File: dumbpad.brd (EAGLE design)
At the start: 98 x 80 mm, 38 parts

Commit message: shrinking, aligning
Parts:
- moved D4 0.52 mm to (89.2, 77.0)
- moved D3 0.51 mm to (70.1, 77.0)
- moved D2 0.50 mm to (51.0, 77.0)
- moved D1 0.50 mm to (32.0, 77.0)
- moved D8 0.18 mm to (89.2, 58.6)
- moved D12 0.16 mm to (89.2, 39.5)
- moved D16 0.15 mm to (89.2, 20.5)
- moved D7 0.14 mm to (70.1, 58.6)
- moved D6 0.11 mm to (51.0, 58.6)
- moved D11 0.11 mm to (70.1, 39.5)
- moved D5 0.10 mm to (32.0, 58.6)
- moved D15 0.10 mm to (70.1, 20.5)
- moved D10 0.07 mm to (51.0, 39.5)
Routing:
- net N$1: track 12.9 -> 12.4 mm
- net N$2: track 12.9 -> 12.4 mm
- net N$3: track 12.9 -> 12.4 mm
- net N$4: track 12.9 -> 12.4 mm
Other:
- board size 98 x 80 mm -> 98 x 79.5 mm

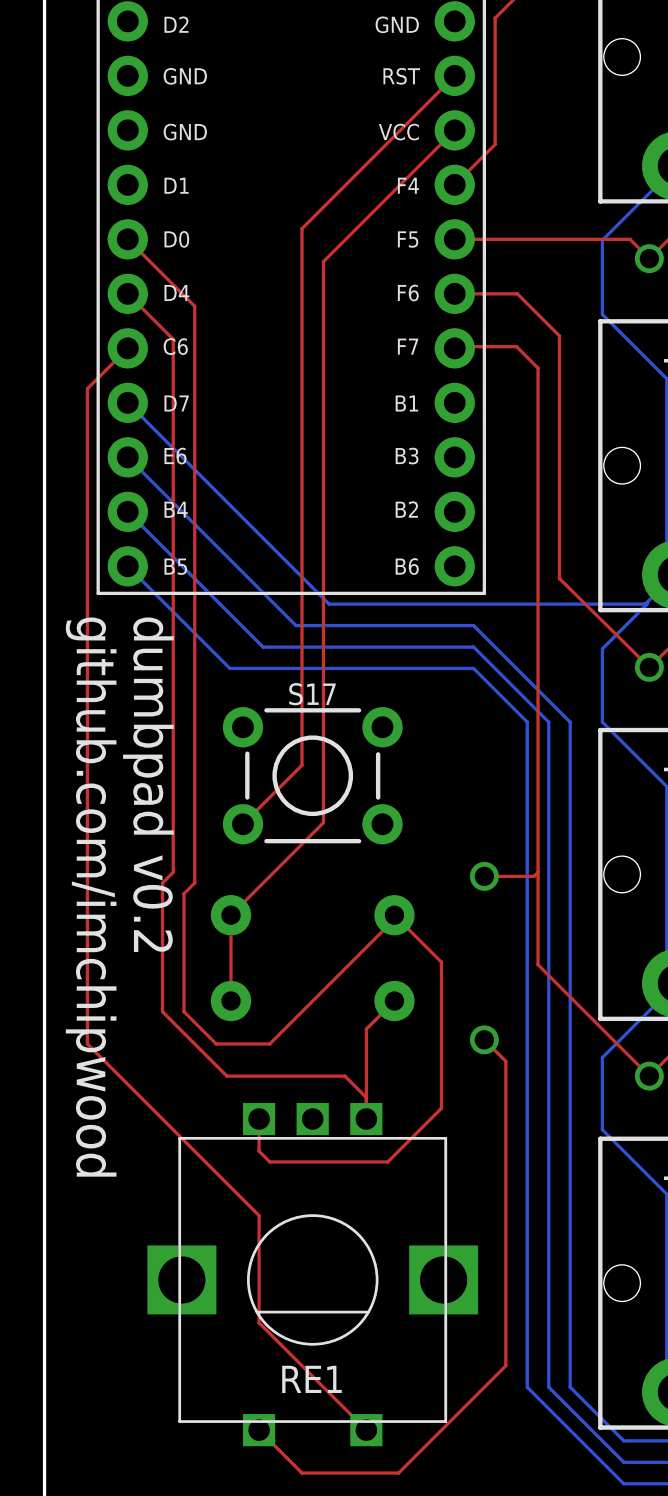
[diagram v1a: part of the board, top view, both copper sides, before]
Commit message: removed resistors from rotary encoder, updated readme
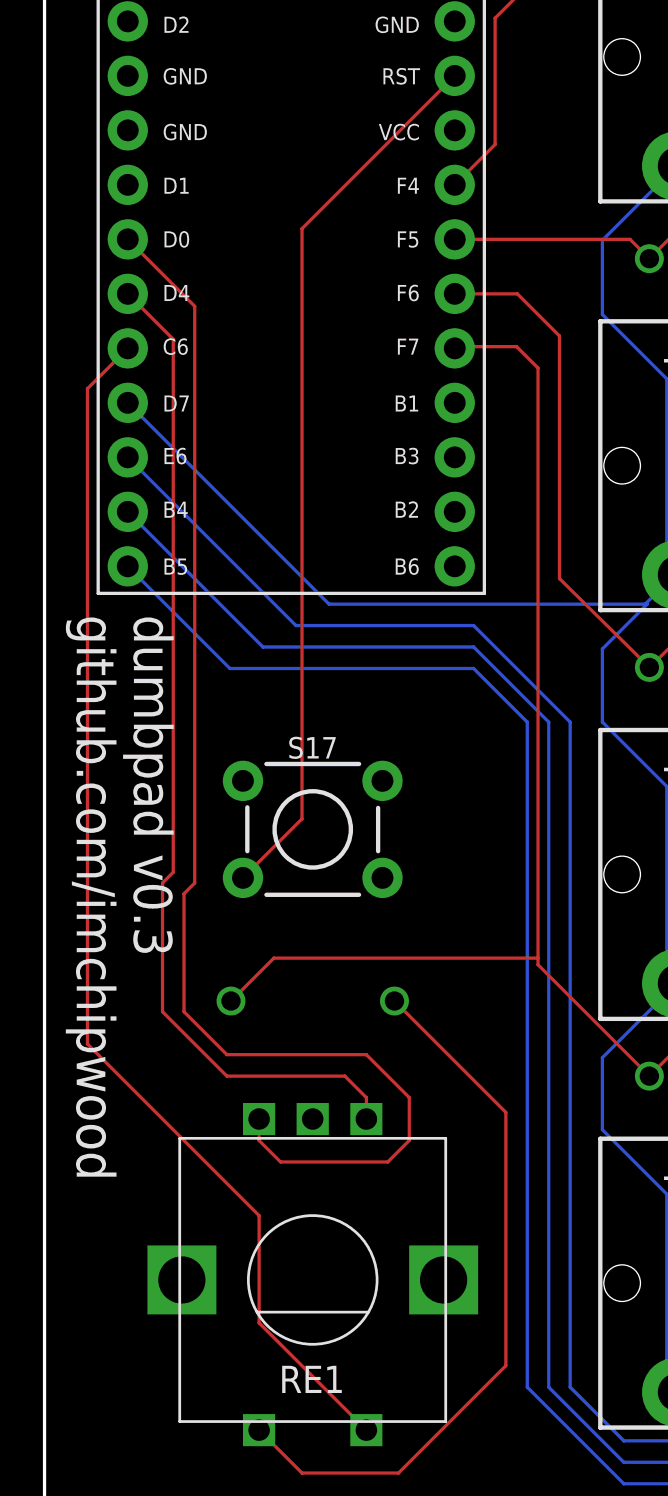
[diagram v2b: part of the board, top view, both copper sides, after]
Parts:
- removed R1, R2: 10k, SparkFun-Resistors:AXIAL-0.3
- moved D17 8.25 mm to (12.5, 24.0), turned to 0 degrees
- moved S17 2.50 mm to (12.5, 32.0)
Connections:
- net ENCODER_L0: no longer R1.P$1
- net ENCODER_L1: no longer R2.P$1
- net VCC: no longer R1.P$2, R2.P$2
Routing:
- net VCC: track 44.9 -> 0.00 mm
- net ROW3: track 102.9 -> 115.5 mm
- net ENCODER_L1: track 71.7 -> 60.5 mm
- net ENCODER_L0: track 52.7 -> 46.7 mm
- net N$10: track 30.0 -> 33.5 mm
- net RESET: track 39.0 -> 41.5 mm
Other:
- board text added: "dumbpad v0.3 github.com/imchipwood"
- board text removed: "dumbpad v0.2 github.com/imchipwood"
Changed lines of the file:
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@@
 <wire x1="0" y1="0" x2="98" y2="0" width="0.1524" layer="20"/>
 <wire x1="98" y1="0" x2="98" y2="79.5" width="0.1524" layer="20"/>
-<text x="1.5" y="42" size="1.778" layer="25" rot="SR270">dumbpad v0.2
+<text x="1.5" y="42" size="1.778" layer="25" rot="SR270">dumbpad v0.3
 github.com/imchipwood</text>
 <wire x1="2.5" y1="76" x2="7.5" y2="76" width="0.1524" layer="21"/>
@@
 <wire x1="15.5" y1="77.5" x2="15.5" y2="76" width="0.1524" layer="21"/>
 <text x="11.5" y="73.5" size="1.778" layer="21" align="bottom-center">pro micro</text>
-<text x="1.5" y="16" size="1.778" layer="26" rot="SMR90">dumbpad v0.2
+<text x="1.5" y="16" size="1.778" layer="26" rot="SMR90">dumbpad v0.3
 github.com/imchipwood</text>
 <text x="17.5" y="69.5" size="0.75" layer="21" align="center-right">GND</text>
@@
 <attribute name="VALUE" x="91.182" y="20.246" size="0.6096" layer="22" rot="MR0"/>
 </element>
-<element name="R1" library="SparkFun-Resistors" package="AXIAL-0.3" value="10k" x="12.5" y="24" smashed="yes" rot="MR0">
-<attribute name="NAME" x="12.5" y="25.016" size="1" layer="26" font="vector" ratio="20" rot="MR0" align="bottom-center"/>
-<attribute name="PROD_ID" value="RES-12183" x="12.5" y="24" size="1.778" layer="28" rot="MR0" display="off"/>
-<attribute name="VALUE" x="12.5" y="22.984" size="0.6096" layer="28" font="vector" ratio="20" rot="MR0" align="top-center"/>
-</element>
-<element name="R2" library="SparkFun-Resistors" package="AXIAL-0.3" value="10k" x="12.5" y="28" smashed="yes" rot="MR0">
-<attribute name="NAME" x="12.5" y="29.016" size="1" layer="26" font="vector" ratio="20" rot="MR0" align="bottom-center"/>
-<attribute name="PROD_ID" value="RES-12183" x="12.5" y="28" size="1.778" layer="28" rot="MR0" display="off"/>
-<attribute name="VALUE" x="12.5" y="26.984" size="0.6096" layer="28" font="vector" ratio="20" rot="MR0" align="top-center"/>
-</element>
-<element name="S17" library="SparkFun-Switches" package="TACTILE_SWITCH_PTH_6.0MM" value="MOMENTARY-SWITCH-SPST-PTH-6.0MM" x="12.5" y="34.5" smashed="yes">
-<attribute name="NAME" x="12.5" y="37.802" size="1" layer="25" font="vector" ratio="20" align="bottom-center"/>
-<attribute name="PROD_ID" value=" SWCH-08441" x="12.5" y="34.5" size="1.778" layer="27" display="off"/>
-<attribute name="SF_SKU" value="COM-00097" x="12.5" y="34.5" size="1.778" layer="27" display="off"/>
-<attribute name="VALUE" x="12.5" y="31.325" size="0.6096" layer="27" font="vector" ratio="20" align="top-center"/>
-</element>
-<element name="D17" library="adafruit" package="DO-1N4148" value="" x="20.5" y="26" smashed="yes" rot="MR90">
-<attribute name="NAME" x="21.77" y="25.96" size="1" layer="26" rot="MR90" align="bottom-center"/>
-<attribute name="VALUE" x="20.246" y="23.968" size="0.6096" layer="22" rot="MR90"/>
+<element name="S17" library="SparkFun-Switches" package="TACTILE_SWITCH_PTH_6.0MM" value="MOMENTARY-SWITCH-SPST-PTH-6.0MM" x="12.5" y="32" smashed="yes">
+<attribute name="NAME" x="12.5" y="35.302" size="1" layer="25" font="vector" ratio="20" align="bottom-center"/>
+<attribute name="PROD_ID" value=" SWCH-08441" x="12.5" y="32" size="1.778" layer="27" display="off"/>
+<attribute name="SF_SKU" value="COM-00097" x="12.5" y="32" size="1.778" layer="27" display="off"/>
+<attribute name="VALUE" x="12.5" y="28.825" size="0.6096" layer="27" font="vector" ratio="20" align="top-center"/>
+</element>
+<element name="D17" library="adafruit" package="DO-1N4148" value="" x="12.5" y="24" smashed="yes" rot="MR0">
+<attribute name="NAME" x="12.54" y="25.27" size="1" layer="26" rot="MR0" align="bottom-center"/>
+<attribute name="VALUE" x="14.532" y="23.746" size="0.6096" layer="22" rot="MR0"/>
 </element>
 </elements>
@@
 <contactref element="RE1" pad="A"/>
 <contactref element="B1" pad="7"/>
-<contactref element="R1" pad="P$1"/>
-<wire x1="15" y1="18.5" x2="15" y2="22.69" width="0.1524" layer="1"/>
-<wire x1="15" y1="22.69" x2="16.31" y2="24" width="0.1524" layer="1"/>
 <wire x1="15" y1="18.5" x2="15" y2="19.5" width="0.1524" layer="1"/>
 <wire x1="15" y1="19.5" x2="14" y2="20.5" width="0.1524" layer="1"/>
@@
 <contactref element="B1" pad="6"/>
 <contactref element="RE1" pad="B"/>
-<contactref element="R2" pad="P$1"/>
-<wire x1="10" y1="18.5" x2="10" y2="17" width="0.1524" layer="1"/>
-<wire x1="10" y1="17" x2="10.5" y2="16.5" width="0.1524" layer="1"/>
-<wire x1="10.5" y1="16.5" x2="16" y2="16.5" width="0.1524" layer="1"/>
-<wire x1="16" y1="16.5" x2="18.5" y2="19" width="0.1524" layer="1"/>
-<wire x1="18.5" y1="19" x2="18.5" y2="25.81" width="0.1524" layer="1"/>
-<wire x1="18.5" y1="25.81" x2="16.31" y2="28" width="0.1524" layer="1"/>
-<wire x1="16.31" y1="28" x2="16.31" y2="27.81" width="0.1524" layer="1"/>
-<wire x1="16.31" y1="27.81" x2="10.5" y2="22" width="0.1524" layer="1"/>
-<wire x1="10.5" y1="22" x2="8" y2="22" width="0.1524" layer="1"/>
-<wire x1="8" y1="22" x2="6.5" y2="23.5" width="0.1524" layer="1"/>
+<wire x1="6.5" y1="23.5" x2="8.5" y2="21.5" width="0.1524" layer="1"/>
 <wire x1="6.5" y1="23.5" x2="6.5" y2="29" width="0.1524" layer="1"/>
 <wire x1="6.5" y1="29" x2="7" y2="29.5" width="0.1524" layer="1"/>
 <wire x1="7" y1="29.5" x2="7" y2="56.38" width="0.1524" layer="1"/>
 <wire x1="7" y1="56.38" x2="3.88" y2="59.5" width="0.1524" layer="1"/>
+<wire x1="15" y1="21.5" x2="17" y2="19.5" width="0.1524" layer="1"/>
+<wire x1="17" y1="19.5" x2="17" y2="17.5" width="0.1524" layer="1"/>
+<wire x1="17" y1="17.5" x2="16" y2="16.5" width="0.1524" layer="1"/>
+<wire x1="16" y1="16.5" x2="11" y2="16.5" width="0.1524" layer="1"/>
+<wire x1="11" y1="16.5" x2="10" y2="17.5" width="0.1524" layer="1"/>
+<wire x1="10" y1="17.5" x2="10" y2="18.5" width="0.1524" layer="1"/>
+<wire x1="8.5" y1="21.5" x2="15" y2="21.5" width="0.1524" layer="1"/>
 </signal>
 <signal name="ROW0">
@@
 <wire x1="19.2" y1="54.5" x2="19.12" y2="54.42" width="0.1524" layer="1"/>
 <contactref element="D17" pad="C"/>
-<wire x1="23" y1="30" x2="23" y2="53.5" width="0.1524" layer="1"/>
-<wire x1="20.5" y1="29.81" x2="22.81" y2="29.81" width="0.1524" layer="1"/>
-<wire x1="22.81" y1="29.81" x2="23" y2="30" width="0.1524" layer="1"/>
+<wire x1="23" y1="25.69" x2="23" y2="26" width="0.1524" layer="1"/>
+<wire x1="23" y1="26" x2="23" y2="53.5" width="0.1524" layer="1"/>
 <wire x1="66.29" y1="20.5" x2="67.79" y2="22" width="0.1524" layer="1"/>
 <wire x1="83.84" y1="22" x2="85.34" y2="20.5" width="0.1524" layer="1"/>
@@
 <wire x1="45.74" y1="22" x2="29.69" y2="22" width="0.1524" layer="1"/>
 <wire x1="28.19" y1="20.5" x2="23" y2="25.69" width="0.1524" layer="1"/>
-<wire x1="23" y1="25.69" x2="23" y2="30" width="0.1524" layer="1"/>
+<wire x1="8.69" y1="24" x2="10.69" y2="26" width="0.1524" layer="1"/>
+<wire x1="10.69" y1="26" x2="23" y2="26" width="0.1524" layer="1"/>
 </signal>
 <signal name="VCC">
 <contactref element="B1" pad="21"/>
-<contactref element="R1" pad="P$2"/>
-<contactref element="R2" pad="P$2"/>
-<wire x1="8.69" y1="24" x2="8.69" y2="28" width="0.1524" layer="1"/>
-<wire x1="8.69" y1="28" x2="13" y2="32.31" width="0.1524" layer="1"/>
-<wire x1="13" y1="58.46" x2="19.12" y2="64.58" width="0.1524" layer="1"/>
-<wire x1="13" y1="32.31" x2="13" y2="58.46" width="0.1524" layer="1"/>
 </signal>
 <signal name="N$1">
@@
 <contactref element="B1" pad="22"/>
 <contactref element="S17" pad="3"/>
-<wire x1="9.2488" y1="32.2394" x2="12" y2="34.9906" width="0.1524" layer="1"/>
+<wire x1="9.2488" y1="29.7394" x2="12" y2="32.4906" width="0.1524" layer="1"/>
 <wire x1="12" y1="60" x2="19.12" y2="67.12" width="0.1524" layer="1"/>
-<wire x1="12" y1="34.9906" x2="12" y2="60" width="0.1524" layer="1"/>
+<wire x1="12" y1="32.4906" x2="12" y2="60" width="0.1524" layer="1"/>
 </signal>
 <signal name="N$10">
@@
 <wire x1="12" y1="2" x2="16.5" y2="2" width="0.1524" layer="1"/>
 <wire x1="16.5" y1="2" x2="21.5" y2="7" width="0.1524" layer="1"/>
-<wire x1="21.5" y1="21.19" x2="21.5" y2="7" width="0.1524" layer="1"/>
-<wire x1="20.5" y1="22.19" x2="21.5" y2="21.19" width="0.1524" layer="1"/>
+<wire x1="21.5" y1="7" x2="21.5" y2="18.81" width="0.1524" layer="1"/>
+<wire x1="21.5" y1="18.81" x2="16.31" y2="24" width="0.1524" layer="1"/>
 </signal>
 <signal name="COL4">

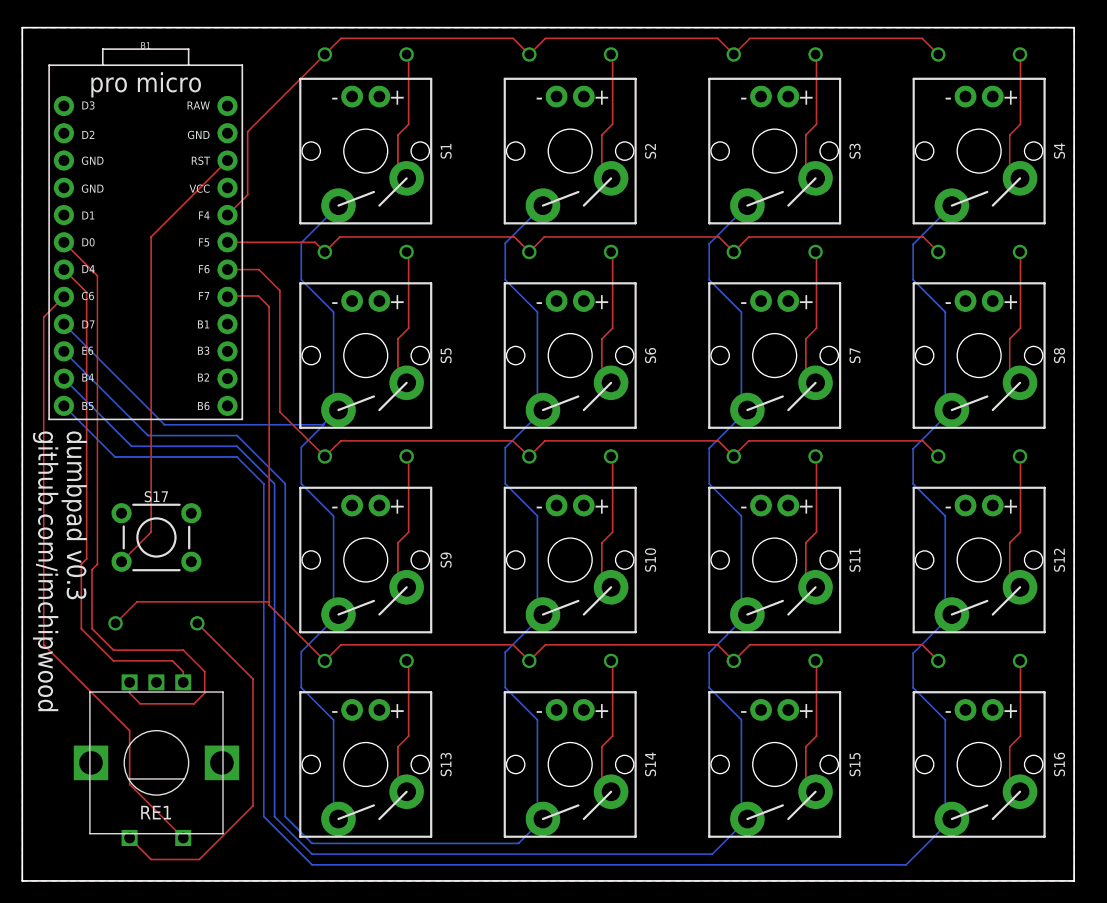
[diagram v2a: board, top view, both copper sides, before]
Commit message: moved all components to top, rerouted
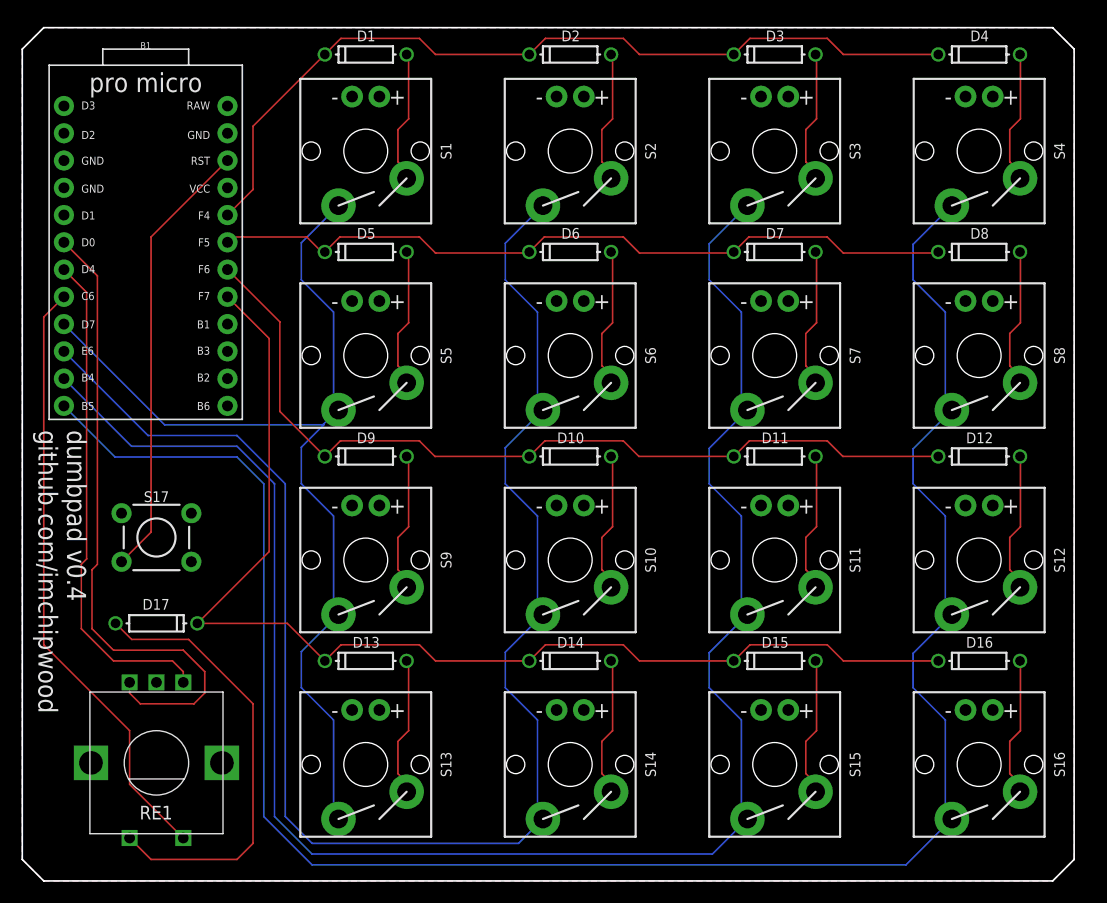
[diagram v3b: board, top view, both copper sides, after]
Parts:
- flipped D1 to the top, turned to 180 degrees
- flipped D10 to the top, turned to 180 degrees
- flipped D11 to the top, turned to 180 degrees
- flipped D12 to the top, turned to 180 degrees
- flipped D13 to the top, turned to 180 degrees
- flipped D14 to the top, turned to 180 degrees
- flipped D15 to the top, turned to 180 degrees
- flipped D16 to the top, turned to 180 degrees
- flipped D17 to the top
- flipped D2 to the top, turned to 180 degrees
- flipped D3 to the top, turned to 180 degrees
- flipped D4 to the top, turned to 180 degrees
- flipped D5 to the top, turned to 180 degrees
- flipped D6 to the top, turned to 180 degrees
- flipped D7 to the top, turned to 180 degrees
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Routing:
- net N$10: track 33.5 -> 41.9 mm
- net ROW3: track 115.5 -> 109.0 mm
- net ROW2: track 83.6 -> 81.9 mm
- net ROW1: track 70.1 -> 70.7 mm
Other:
- outline, holes or cut-outs redrawn
- board text added: "dumbpad v0.4 github.com/imchipwood"
- board text removed: "dumbpad v0.3 github.com/imchipwood"

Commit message: slight tweaks to spacing, orientation of one diode, etc.
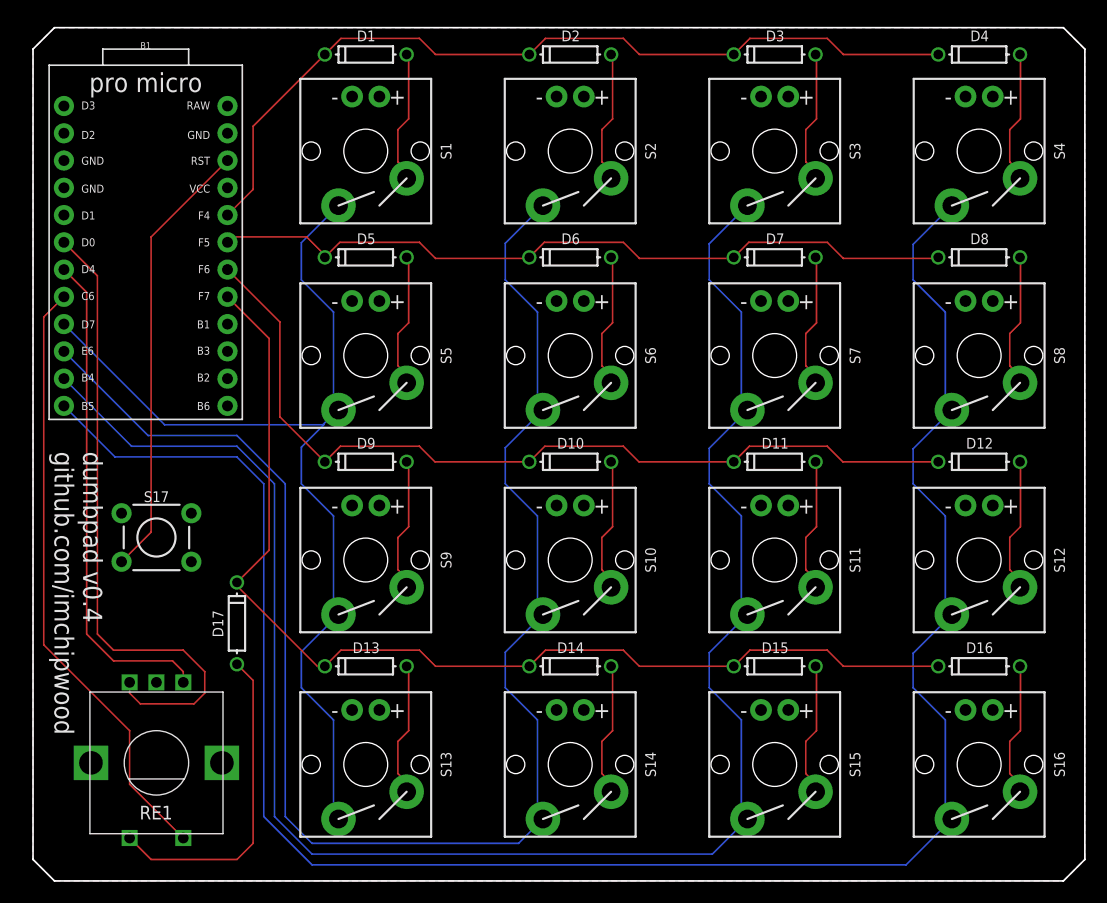
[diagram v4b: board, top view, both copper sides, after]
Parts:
- moved D17 7.50 mm to (20.0, 24.0), turned to 90 degrees
- moved D10 0.50 mm to (51.0, 39.0)
- moved D11 0.50 mm to (70.1, 39.0)
- moved D12 0.50 mm to (89.2, 39.0)
- moved D13 0.50 mm to (32.0, 20.0)
- moved D14 0.50 mm to (51.0, 20.0)
- moved D15 0.50 mm to (70.1, 20.0)
- moved D16 0.50 mm to (89.2, 20.0)
- moved D5 0.50 mm to (32.0, 58.1)
- moved D6 0.50 mm to (51.0, 58.1)
- moved D7 0.50 mm to (70.1, 58.1)
- moved D8 0.50 mm to (89.2, 58.1)
- moved D9 0.50 mm to (32.0, 39.0)
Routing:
- net N$10: track 41.9 -> 30.3 mm
- net ROW3: track 109.0 -> 101.9 mm
- net ROW2: track 81.9 -> 82.4 mm
- net N$9: track 13.0 -> 12.5 mm
- net N$8: track 13.0 -> 12.5 mm
- net N$7: track 13.0 -> 12.5 mm
- net N$6: track 13.0 -> 12.5 mm
- net N$19: track 13.0 -> 12.5 mm
- net N$18: track 13.0 -> 12.5 mm
- net N$17: track 13.0 -> 12.5 mm
- net N$16: track 13.0 -> 12.5 mm
- net N$14: track 13.0 -> 12.5 mm
- net N$13: track 13.0 -> 12.5 mm
- net N$12: track 13.0 -> 12.5 mm
- net N$11: track 13.0 -> 12.5 mm
